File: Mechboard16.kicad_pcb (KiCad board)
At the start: 2 copper layers, 386.1 x 97 mm, 240 parts, among them CN1 CONN_C16, CN2 CONN_+4, J201 USB_B, J202 CONN_ICSP, J203 CONN_MRESET, SW0:0 KEY_DEL, SW0:1 KEY_RET, SW0:2 KEY_PND, SW0:3 KEY_HLP, SW0:4 KEY_F1, SW0:5 KEY_F2, SW0:6 KEY_F3, SW0:7 KEY_AT, SW1:0 KEY_3, SW1:1 KEY_W, SW1:2 KEY_A, SW1:3 KEY_4, SW1:4 KEY_Z, SW1:5 KEY_S, SW1:6 KEY_E, SW1:7 KEY_LSH, SW1B:7 KEY_RSH, SW1C:7 KEY_CLK, SW201 SW_RESET, SW2:0 KEY_5, SW2:1 KEY_R, SW2:2 KEY_D, SW2:3 KEY_6, SW2:4 KEY_C, SW2:5 KEY_F, SW2:6 KEY_T, SW2:7 KEY_X, SW3:0 KEY_7, SW3:1 KEY_Y, SW3:2 KEY_G, SW3:3 KEY_8, SW3:4 KEY_B, SW3:5 KEY_H, SW3:6 KEY_U, SW3:7 KEY_V, SW4:0 KEY_9, SW4:1 KEY_I, SW4:2 KEY_J, SW4:3 KEY_0, SW4:4 KEY_M, SW4:5 KEY_K, SW4:6 KEY_O, SW4:7 KEY_N, SW5:0 KEY_DN, SW5:1 KEY_P, SW5:2 KEY_L, SW5:3 KEY_UP, SW5:4 KEY_DOT, SW5:5 KEY_COL, SW5:6 KEY_MIN, SW5:7 KEY_COM, SW6:0 KEY_LF, SW6:1 KEY_AST, SW6:2 KEY_SEM, SW6:3 KEY_RT, SW6:4 KEY_ESC, SW6:5 KEY_EQ, SW6:6 KEY_PLS, SW6:7 KEY_SLA, SW7:0 KEY_1, SW7:1 KEY_CLR, SW7:2 KEY_CTL, SW7:3 KEY_2, SW7:4 KEY_SPC, SW7:5 KEY_CMD, SW7:6 KEY_Q, SW7:7 KEY_RUN, U1 4066, U2 NE555, U201 ATmega32U4-AU, Y1 16M

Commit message: WIP
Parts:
- removed C211: 100n, Capacitor_SMD:C_0805_2012Metric_Pad1.18x1.45mm_HandSolder
- added U202: MAX7221xWG, Package_SO:SOIC-24W_7.5x15.4mm_P1.27mm, B.Cu at (353.2, 44.0)
- added Y201: 16M, Crystal:Crystal_HC49-4H_Vertical, B.Cu at (397.0, 109.1)
- SW201: footprint Button_Switch_THT:SW_PUSH_6mm -> Button_Switch_SMD:SW_SPST_EVPBF
- moved J201 115.1 mm to (392.9, 39.2), turned to 270 degrees
- moved C210 112.7 mm to (351.5, 51.6), turned to 180 degrees
- moved R205 99.4 mm to (355.7, 51.6), turned to 0 degrees
- moved R202 87.1 mm to (395.4, 57.4), turned to 90 degrees
- moved J202 82.1 mm to (400.8, 74.0), turned to 180 degrees
- moved R203 81.0 mm to (392.9, 57.4), turned to 90 degrees
- moved D201 74.7 mm to (399.5, 69.0), turned to 180 degrees
- moved C207 70.3 mm to (393.7, 84.4), turned to 90 degrees
- moved C203 65.7 mm to (401.3, 83.8), turned to 90 degrees
- moved C208 63.5 mm to (387.7, 84.4), turned to 90 degrees
- moved C204 61.1 mm to (397.5, 83.9), turned to 90 degrees
- moved C205 54.2 mm to (389.5, 104.9)
- moved C209 51.0 mm to (383.8, 89.3), turned to 90 degrees
- moved C202 45.6 mm to (402.8, 104.0), turned to 90 degrees
- moved C206 43.8 mm to (402.8, 99.6), turned to 270 degrees
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- renumbered Y1 to Y202
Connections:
- U201 pad 39: Net-(U201-Pad39) -> /USB Controller/soft_ss
- U201 pad 40: Net-(U201-Pad40) -> /USB Controller/soft_sck
- U201 pad 41: Net-(U201-Pad41) -> /USB Controller/soft_mosi
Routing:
- net /USB Controller/lrow1: track 155.9 -> 405.1 mm, vias 0 -> 1
- net /USB Controller/lrow2: track 154.6 -> 364.0 mm, vias 0 -> 1
- net /USB Controller/lrow6: track 414.5 -> 505.5 mm, vias 2 -> 3
- net /USB Controller/lrow4: track 154.7 -> 229.7 mm, vias 0 -> 1
- net /USB Controller/soft_ss: track 0.00 -> 69.8 mm
- net row1: track 496.7 -> 564.2 mm, vias 3 -> 4
- net /USB Controller/soft_sck: track 0.00 -> 64.6 mm
- net +5V: track 422.5 -> 484.7 mm, vias 4 -> 7
- net /USB Controller/lrow5: track 189.4 -> 245.8 mm, vias 1 -> 2
- net /USB Controller/lcol2: track 292.2 -> 348.4 mm
- net col7: track 410.3 -> 457.6 mm, vias 6 -> 7
- net /USB Controller/lcol5: track 329.3 -> 373.5 mm
- net VCC: track 0.00 -> 41.2 mm
- net /USB Controller/usb+: track 0.00 -> 32.6 mm
- net /USB Controller/usb-: track 0.00 -> 32.4 mm
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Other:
- board text added: "ICSP"

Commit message: WIP2
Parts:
- U202: value MAX7221xWG -> MAX7221
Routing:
- net /USB Controller/lrow3: track 154.8 -> 334.7 mm, vias 0 -> 3
- net /USB Controller/lcol4: track 444.5 -> 329.9 mm, vias 2 -> 1
- net /USB Controller/lcol7: track 310.9 -> 418.7 mm, vias 1 -> 2
- net /USB Controller/lcol3: track 216.5 -> 289.2 mm
- net /USB Controller/lcol1: track 313.0 -> 362.3 mm, vias 1 -> 2
- net /USB Controller/lrow4: track 229.7 -> 278.1 mm
- net /USB Controller/lrow7: track 428.6 -> 474.6 mm, vias 1 -> 3
- net col3: track 467.4 -> 428.8 mm, vias 4 -> 6
- net /USB Controller/lcol5: track 373.5 -> 410.1 mm, vias 2 -> 3
- net /USB Controller/soft_mosi: track 0.00 -> 16.5 mm
- net GND: track 398.7 -> 407.8 mm, vias 1 -> 3
- net /USB Controller/lrow2: track 364.0 -> 358.1 mm
- net /USB Controller/lrow6: track 505.5 -> 503.8 mm
- net /USB Controller/lcol0: track 304.6 -> 306.1 mm
- net /USB Controller/lrow1: track 405.1 -> 403.6 mm
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
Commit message: I'm tired and I want to go to bed
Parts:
- moved C209 1.02 mm to (382.8, 89.3)
- moved R201 0.19 mm to (382.8, 109.7)
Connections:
- U201 pad 39: /USB Controller/soft_ss -> /USB Controller/soft_sck
- U201 pad 40: /USB Controller/soft_sck -> /USB Controller/soft_mosi
- U201 pad 41: /USB Controller/soft_mosi -> /USB Controller/soft_ss
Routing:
- net /USB Controller/lcol4: track 329.9 -> 473.8 mm, vias 1 -> 5
- net /USB Controller/lcol6: track 259.3 -> 370.0 mm, vias 0 -> 2
- net /USB Controller/lcol3: track 289.2 -> 369.6 mm, vias 0 -> 2
- net /USB Controller/soft_mosi: track 16.5 -> 86.6 mm
- net row6: track 505.6 -> 573.4 mm, vias 3 -> 4
- net +5V: track 484.7 -> 534.0 mm, vias 7 -> 10
- net /USB Controller/lcol2: track 347.7 -> 387.5 mm, vias 2 -> 5
- net /USB Controller/lcol5: track 410.1 -> 447.5 mm, vias 3 -> 5
- net /USB Controller/lrow0: track 253.8 -> 271.3 mm, vias 1 -> 2
- net GND: track 407.8 -> 417.2 mm, vias 3 -> 5
- net /USB Controller/~reset: track 3.16 -> 8.92 mm
- net /USB Controller/soft_ss: track 69.8 -> 74.6 mm
- net /USB Controller/soft_sck: track 64.6 -> 69.2 mm
- net /USB Controller/lcol7: track 418.7 -> 417.5 mm
- net /USB Controller/lrow6: track 503.8 -> 504.9 mm, vias 3 -> 2
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
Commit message: I need to drink more than you seem to think
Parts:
- J203: moved to B.Cu
- moved J203 83.9 mm to (383.7, 67.8)
- moved C209 1.59 mm to (382.8, 90.9)
- moved R201 0.22 mm to (383.0, 109.7)
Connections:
- U201 pad 31: /USB Controller/~mreset -> Net-(U201-Pad31)
- U201 pad 38: Net-(U201-Pad38) -> /USB Controller/soft_sck
- U201 pad 39: /USB Controller/soft_sck -> /USB Controller/soft_mosi
- U201 pad 40: /USB Controller/soft_mosi -> /USB Controller/soft_ss
- U201 pad 41: /USB Controller/soft_ss -> /USB Controller/~mreset
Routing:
- net +5V: track 534.0 -> 597.5 mm, vias 10 -> 11
- net /USB Controller/~mreset: track 0.00 -> 24.5 mm
- net row6: track 573.4 -> 576.7 mm
- net row5: track 398.6 -> 401.9 mm
- net row4: track 391.5 -> 394.8 mm
- net row0: track 373.3 -> 375.2 mm
- net /USB Controller/lrow0: track 271.3 -> 269.9 mm
- net row7: track 608.5 -> 607.7 mm

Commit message: HEEEEEAAAADLOOOOOOOOOOONGGG!
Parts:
- removed LD201: STATUS_LED, LED_SMD:LED_0805_2012Metric_Pad1.15x1.40mm_HandSolder
- added C211: 100n, Capacitor_SMD:C_0805_2012Metric_Pad1.18x1.45mm_HandSolder, B.Cu at (401.3, 84.4)
- added J204: CONN_LED, Connector_PinHeader_2.54mm:PinHeader_1x04_P2.54mm_Vertical, B.Cu at (383.9, 39.2)
- added R205: 1k, Resistor_SMD:R_0805_2012Metric_Pad1.20x1.40mm_HandSolder, B.Cu at (386.2, 57.4)
- added R206: 1k, Resistor_SMD:R_0805_2012Metric_Pad1.20x1.40mm_HandSolder, B.Cu at (383.7, 57.4)
- C203: footprint Capacitor_Tantalum_SMD:CP_EIA-3528-21_Kemet-B_Pad1.50x2.35mm_HandSolder -> Capacitor_THT:CP_Radial_D6.3mm_P2.50mm
- C204: footprint Capacitor_SMD:C_1206_3216Metric_Pad1.33x1.80mm_HandSolder -> Capacitor_THT:CP_Radial_D5.0mm_P2.00mm
- moved R204 70.6 mm to (388.7, 57.4), turned to 270 degrees
- moved J203 47.3 mm to (375.4, 114.3), turned to 270 degrees
- moved C203 38.1 mm to (382.8, 117.1), turned to 0 degrees
- moved C204 1.48 mm to (397.5, 85.4)
- moved R201 0.22 mm to (382.8, 109.7)
- moved R202 0.07 mm to (395.5, 57.4)
- renumbered R205 to R207
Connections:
- R204 pad 2: GND -> /USB Controller/st_led_r
- U201 pad 31: Net-(U201-Pad31) -> /USB Controller/~mreset
- U201 pad 32: /USB Controller/st_led -> Net-(U201-Pad32)
- U201 pad 36: Net-(U201-Pad36) -> /USB Controller/soft_sck
- U201 pad 37: Net-(U201-Pad37) -> /USB Controller/soft_mosi
- U201 pad 38: /USB Controller/soft_sck -> /USB Controller/soft_ss
- U201 pad 39: /USB Controller/soft_mosi -> /USB Controller/st_le_b
- U201 pad 40: /USB Controller/soft_ss -> /USB Controller/st_led_g
- U201 pad 41: /USB Controller/~mreset -> /USB Controller/st_led_r
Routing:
- net GND: track 417.2 -> 466.9 mm, vias 5 -> 4
- net /USB Controller/~reset: track 8.92 -> 54.6 mm, vias 0 -> 3
- net /USB Controller/st_led_r: track 0.00 -> 35.5 mm
- net /USB Controller/st_led_g: track 0.00 -> 35.3 mm
- net /USB Controller/st_le_b: track 0.00 -> 35.1 mm
- net +5V: track 597.5 -> 630.2 mm, vias 11 -> 12
- net row5: track 401.9 -> 375.2 mm
- net Net-(J204-Pad2): track 0.00 -> 16.6 mm
- net /USB Controller/lcol3: track 369.6 -> 386.2 mm, vias 2 -> 1
- net Net-(J204-Pad3): track 0.00 -> 13.1 mm
- net /USB Controller/lcol4: track 473.8 -> 486.1 mm
- net Net-(J204-Pad4): track 0.00 -> 10.2 mm
- net /USB Controller/lcol2: track 387.5 -> 395.2 mm
- net col6: track 439.0 -> 445.1 mm, vias 3 -> 4
- net /USB Controller/lcol6: track 370.0 -> 374.6 mm
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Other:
- board text added: "GND"
- board text added: "RST"

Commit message: Almost there...
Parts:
- moved R201 33.5 mm to (394.0, 78.1)
- moved SW201 33.5 mm to (387.8, 76.2), turned to 270 degrees
- moved C203 8.18 mm to (384.5, 109.1)
- moved C207 0.25 mm to (394.0, 84.4)
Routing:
- net /USB Controller/~reset: track 54.6 -> 40.8 mm
- net GND: track 466.9 -> 476.0 mm
- net +5V: track 630.2 -> 630.1 mm, vias 12 -> 13
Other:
- board text added: "RESET"

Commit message: Done! Just some finishing touches left...
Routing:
- net row7: track 607.7 -> 610.7 mm
- net /USB Controller/~reset: track 40.8 -> 41.8 mm

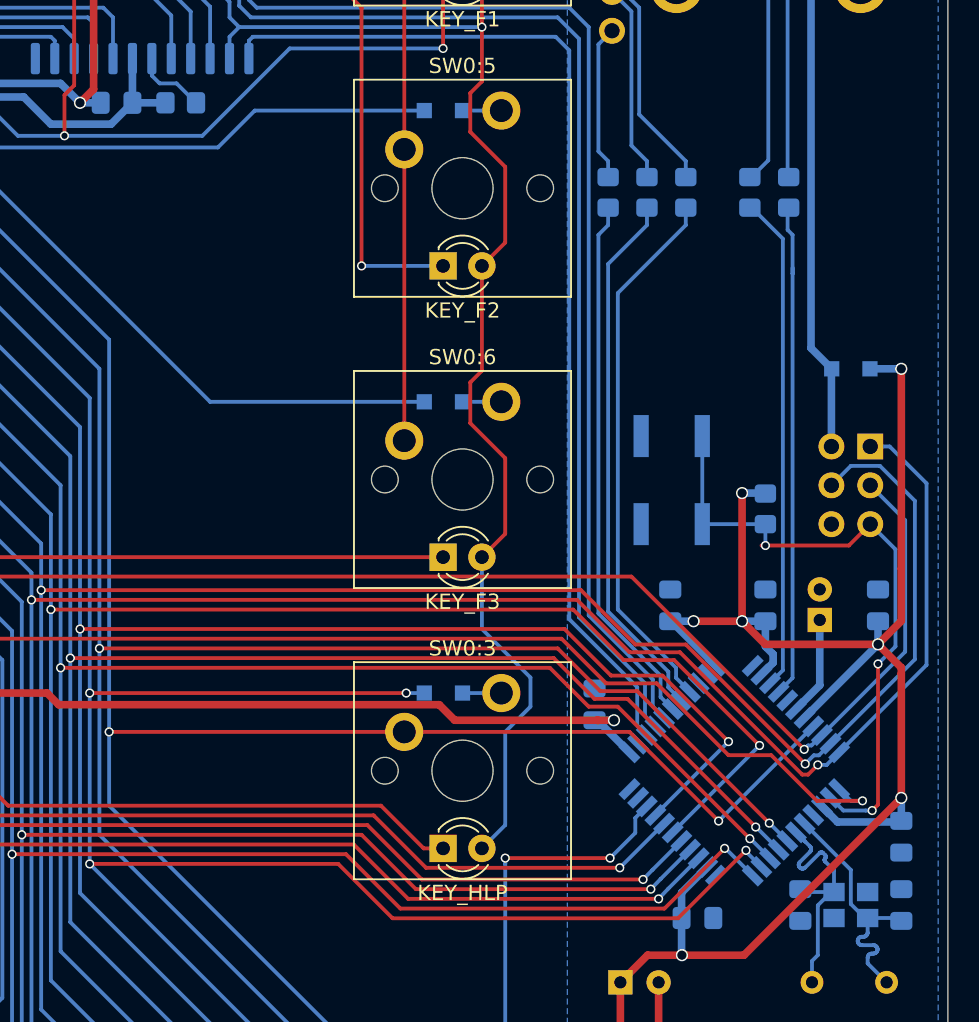
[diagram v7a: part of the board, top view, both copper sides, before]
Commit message: Add legend on J204
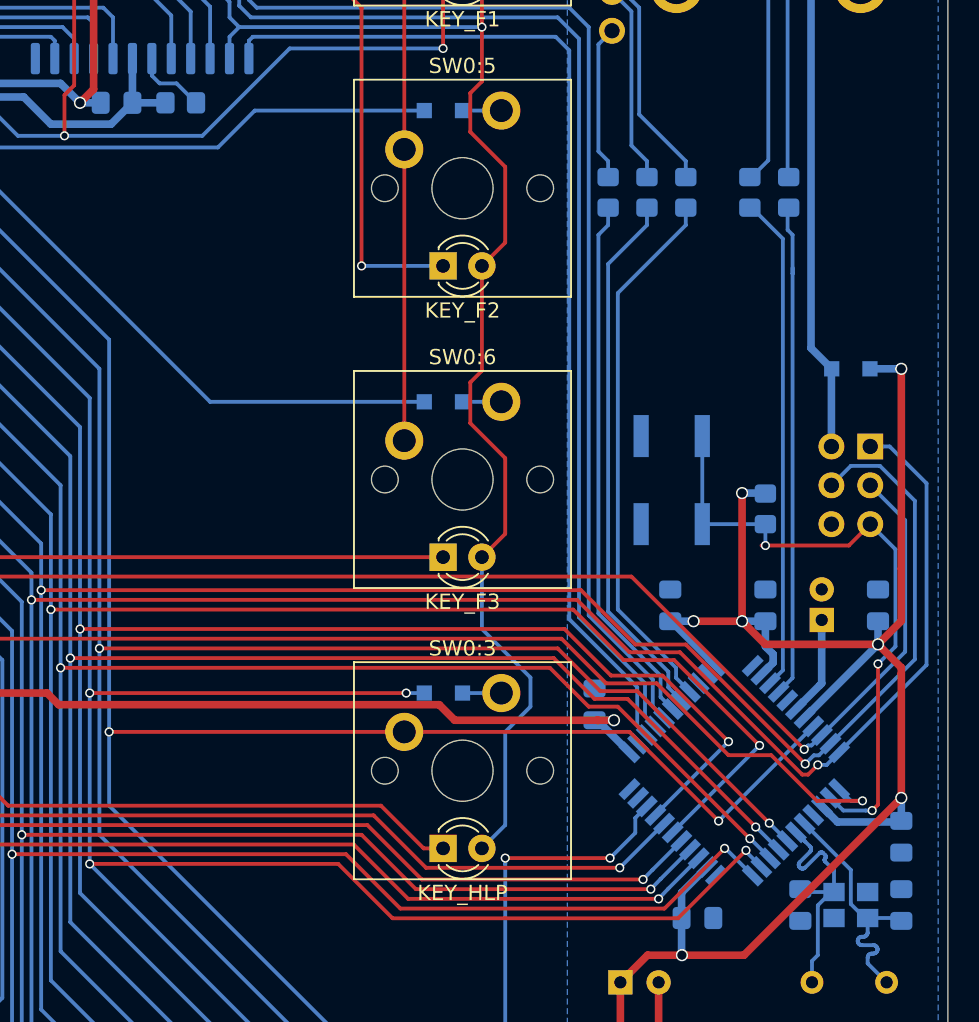
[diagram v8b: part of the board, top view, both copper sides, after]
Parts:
- R207: value TBD -> 22k
- moved C204 0.13 mm to (397.6, 85.4)
